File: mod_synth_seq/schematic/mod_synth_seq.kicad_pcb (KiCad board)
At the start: 2 copper layers, 100.3 x 132.1 mm, 88 parts, among them J1 CV1, J10 Step 8 Gate, J11 Reset, J12 Clock, J13 Gate Out, J2 CV2, J3 Step 1 Gate, J4 Step 2 Gate, J5 Step 3 Gate, J6 Step 4 Gate, J7 Step 5 Gate, J8 Step 6 Gate, J9 Step 7 Gate

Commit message: Update layouts
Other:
- board text added: "DO NOT USE; WRONG SIZE"
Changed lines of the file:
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@@
   (general
     (thickness 1.6)
-    (drawings 8)
+    (drawings 9)
     (tracks 340)
     (zones 0)
@@
     )
   )
+  (gr_text "DO NOT USE; WRONG SIZE" (at 204.47 46.99) (layer F.Cu)
+    (effects (font (size 20 8) (thickness 0.3)))
+  )
   (dimension 10.16 (width 0.12) (layer F.SilkS)

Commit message: Very rough outline of seq PCB
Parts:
- removed REF**: IDC-Header_2x08_P2.54mm_Vertical, Connector_IDC:IDC-Header_2x08_P2.54mm_Vertical
- moved RV17 115.4 mm to (188.0, 126.4), turned to 0 degrees
- moved A1 107.2 mm to (220.3, 41.9), turned to 0 degrees
- moved D17 99.8 mm to (119.9, 49.8)
- moved R12 97.4 mm to (116.3, 113.8)
- moved D33 97.1 mm to (207.0, 59.7), turned to 0 degrees
- moved D34 96.9 mm to (207.0, 43.8), turned to 0 degrees
- moved D21 95.4 mm to (132.7, 49.5)
- moved R20 94.9 mm to (202.2, 33.5), turned to 0 degrees
- moved RV9 94.1 mm to (115.6, 76.2), turned to 0 degrees
- moved R19 94.0 mm to (205.7, 68.6), turned to 0 degrees
- moved D20 93.9 mm to (117.9, 118.4)
- moved RV10 93.0 mm to (116.2, 101.6), turned to 0 degrees
- moved D35 92.2 mm to (194.9, 138.4)
- moved R14 91.2 mm to (127.5, 113.8)
- moved R11 90.8 mm to (116.3, 40.6), turned to 0 degrees
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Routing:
- net GND: track 619.7 -> 0.00 mm
- net Net-(A1-Pad5): track 200.3 -> 0.00 mm
- net Net-(A1-Pad6): track 174.9 -> 0.00 mm
- net Net-(A1-Pad7): track 149.5 -> 0.00 mm
- net Net-(D11-Pad1): track 128.1 -> 0.00 mm
- net Net-(D10-Pad1): track 100.3 -> 0.00 mm
- net Net-(A1-Pad11): track 65.7 -> 0.00 mm
- net Net-(A1-Pad9): track 65.7 -> 0.00 mm
- net Net-(A1-Pad8): track 65.7 -> 0.00 mm
- net Net-(A1-Pad12): track 65.7 -> 0.00 mm
- net Net-(A1-Pad10): track 65.7 -> 0.00 mm
- net Net-(D35-Pad1): track 24.1 -> 0.00 mm
- net Net-(D32-Pad2): track 15.0 -> 0.00 mm
- net Net-(D28-Pad2): track 15.0 -> 0.00 mm
- net Net-(D24-Pad2): track 15.0 -> 0.00 mm
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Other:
- board size 100.3 x 132.1 mm -> 141 x 109.2 mm
- board text removed: "DO NOT USE; WRONG SIZE"

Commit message: Flip components
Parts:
- A1, D10, D11, D12, D14, D15, D16, D18, D19, D2, D20, D22, D23, D24, D26, D27, D28, D3, D30, D31, D32, D33, D34, D35, D4, D6, D7, D8, R1, R10, R11, R12, R13, R14, R15, R16, R17, R18, R19, R2, R20, R21, R3, R4, R5, R6, R7, R8, R9: moved to B.Cu
- moved A1 49.8 mm to (185.4, 77.5)
- moved R9 23.3 mm to (109.2, 37.5)
- moved R13 21.8 mm to (133.3, 37.5)
- moved R15 21.3 mm to (146.7, 37.5)
- moved RV15 12.8 mm to (163.8, 81.3), turned to 90 degrees
- moved J2 12.0 mm to (193.0, 95.2)
- moved J1 11.5 mm to (192.4, 73.7)
- moved RV13 10.6 mm to (149.2, 81.3), turned to 90 degrees
- moved RV7 10.3 mm to (110.5, 83.2), turned to 90 degrees
- moved RV11 10.0 mm to (136.5, 81.3), turned to 90 degrees
- moved RV14 9.94 mm to (149.9, 105.4), turned to 90 degrees
- moved RV16 9.94 mm to (163.2, 105.4), turned to 90 degrees
- moved RV12 9.67 mm to (137.2, 105.4), turned to 90 degrees
- moved RV9 9.53 mm to (123.2, 81.9), turned to 90 degrees
- moved RV3 9.44 mm to (84.5, 83.2), turned to 90 degrees
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
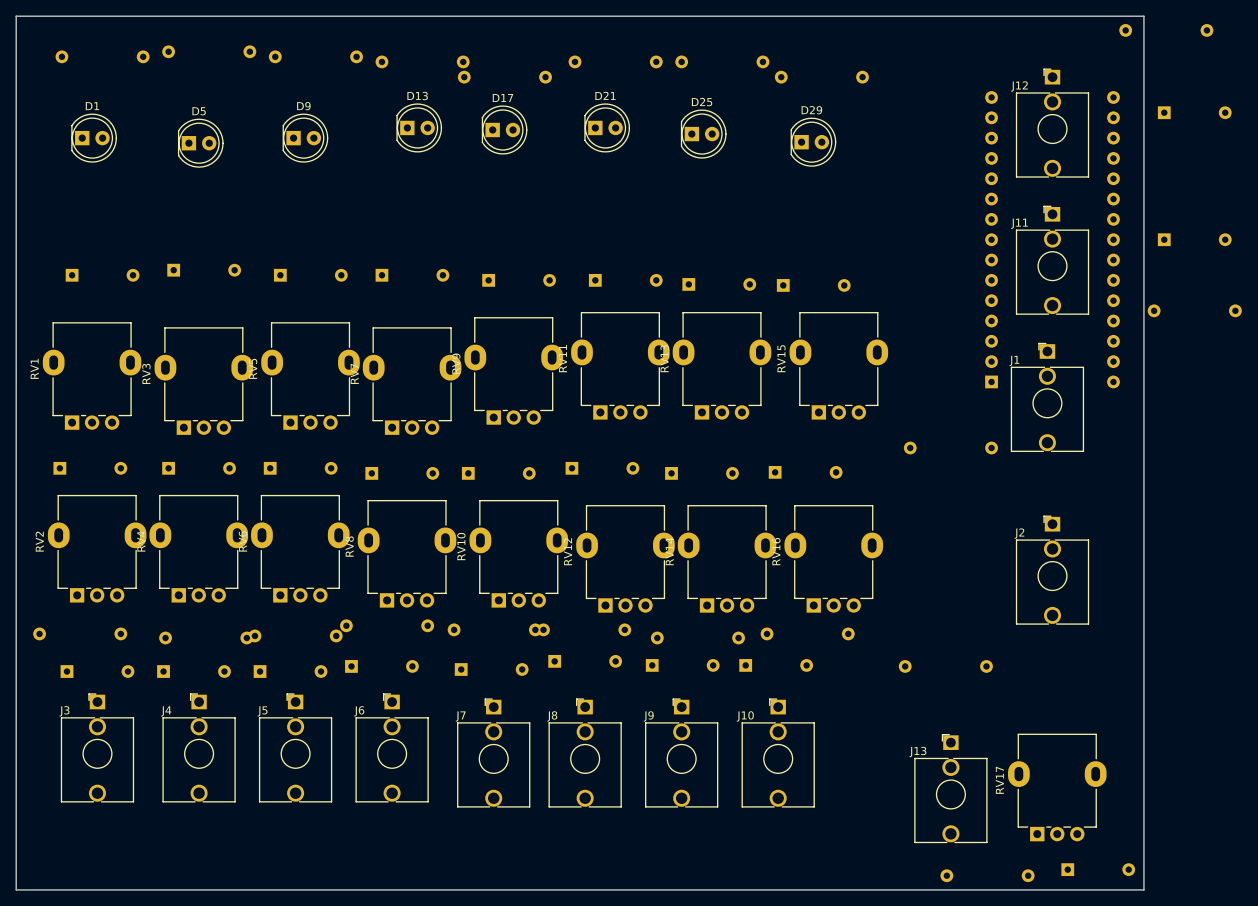
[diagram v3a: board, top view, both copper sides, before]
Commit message: Sequencer board layout
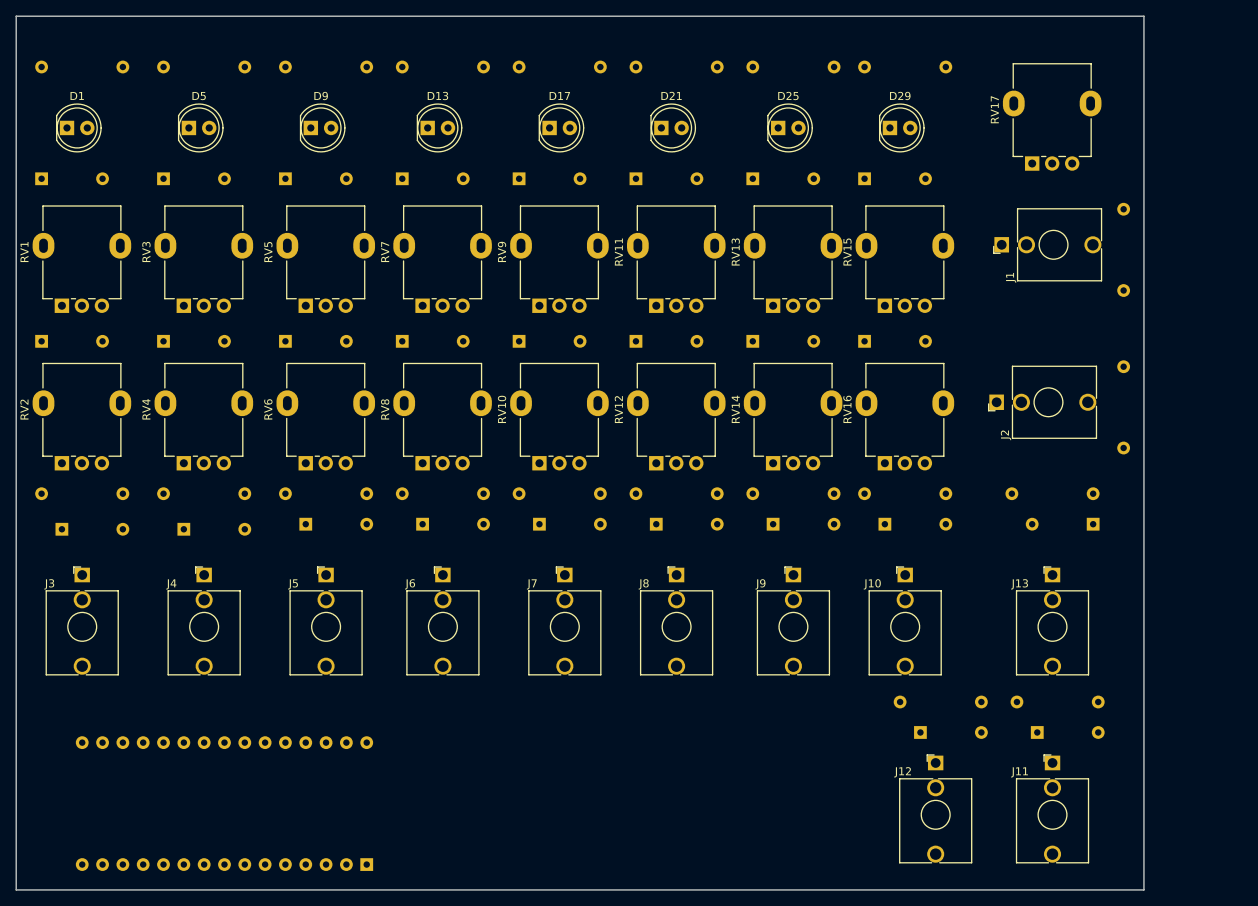
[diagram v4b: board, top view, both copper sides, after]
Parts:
- moved A1 98.7 mm to (107.3, 137.8), turned to 90 degrees
- moved R20 88.6 mm to (174.0, 117.5)
- moved J12 87.0 mm to (178.4, 125.1)
- moved RV17 83.8 mm to (190.5, 50.2)
- moved D34 83.3 mm to (176.5, 121.3)
- moved J11 68.6 mm to (193.0, 125.1)
- moved D33 63.6 mm to (191.1, 121.3)
- moved R19 51.8 mm to (188.6, 117.5)
- moved R21 48.4 mm to (188.0, 91.4)
- moved D35 43.3 mm to (198.1, 95.2), turned to 180 degrees
- moved R2 38.6 mm to (201.9, 85.7), turned to 90 degrees
- moved R1 33.1 mm to (201.9, 66.0), turned to 90 degrees
- moved D32 24.8 mm to (172.1, 95.2)
- moved J13 24.5 mm to (193.0, 101.6)
- moved D28 23.2 mm to (158.1, 95.2)
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
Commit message: Finish sequencer
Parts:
- moved A1 15.5 mm to (104.8, 122.6), turned to 270 degrees
- moved R2 14.7 mm to (187.3, 87.0), turned to 0 degrees
- moved R1 14.0 mm to (188.0, 67.3), turned to 0 degrees
- moved RV17 3.18 mm to (190.5, 53.3)
- moved J7 0.64 mm to (131.4, 101.6)
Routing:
- net +5V: track 0.00 -> 165.1 mm
- net Net-(D10-Pad1): track 0.00 -> 138.5 mm
- net Net-(D11-Pad1): track 0.00 -> 136.9 mm
- net Net-(A1-Pad5): track 0.00 -> 125.6 mm
- net Net-(A1-Pad12): track 0.00 -> 120.2 mm
- net Net-(A1-Pad20): track 0.00 -> 116.8 mm
- net Net-(A1-Pad6): track 0.00 -> 116.2 mm
- net Net-(A1-Pad11): track 0.00 -> 108.4 mm
- net Net-(A1-Pad7): track 0.00 -> 103.1 mm
- net Net-(A1-Pad10): track 0.00 -> 98.5 mm
- net Net-(A1-Pad8): track 0.00 -> 98.3 mm
- net Net-(A1-Pad9): track 0.00 -> 93.5 mm
- net Net-(A1-Pad19): track 0.00 -> 75.4 mm
- net Net-(A1-Pad14): track 0.00 -> 69.2 mm
- net Net-(A1-Pad15): track 0.00 -> 37.4 mm
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- added copper zone on B.Cu, net GND
- added copper zone on F.Cu, net GND
